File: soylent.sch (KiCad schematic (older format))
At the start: 17 parts, among them J1 DB9_Female, J2 Conn_01x04, J3 Conn_01x04, J4 Conn_02x03_Counter_Clockwise, Q1 BC847BPN, U1 ATtiny202-SS, U2 MIC5504-3.3YM5

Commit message: Add explicit jumper wire
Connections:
- net at C2.1, D1.1 (K), D2.1 (K)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: now also JP2.1 (A), U2.3 (EN)
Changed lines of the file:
@@
 	-1   0    0    -1
 $EndComp
-Wire Wire Line
-	7550 5000 7700 5000
 $Comp
 L power:GND #PWR0103
@@
 Wire Wire Line
 	7450 5300 7650 5300
-Wire Wire Line
-	7650 5300 7650 4800
 Connection ~ 7650 4800
 Wire Wire Line
@@
 Wire Wire Line
 	7900 4800 8000 4800
+Wire Wire Line
+	7650 5300 7650 4800
+Wire Wire Line
+	7550 5000 7700 5000
+Wire Wire Line
+	8000 5000 8000 5200
+Wire Wire Line
+	8000 5200 7700 5200
+Wire Wire Line
+	7700 5200 7700 5000
+Connection ~ 8000 5000
+Connection ~ 7700 5000
 $EndSCHEMATC

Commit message: Pick footprints for remaining items
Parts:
- C1, C2: footprint (none) -> Capacitor_SMD:C_0603_1608Metric
- D1, D2: footprint (none) -> Diode_SMD:D_0603_1608Metric
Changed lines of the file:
@@
 F 0 "C2" V 7048 5300 50  0000 C CNN
 F 1 "1u" V 7139 5300 50  0000 C CNN
-F 2 "" H 7338 5150 50  0001 C CNN
+F 2 "Capacitor_SMD:C_0603_1608Metric" H 7338 5150 50  0001 C CNN
 F 3 "~" H 7300 5300 50  0001 C CNN
 	1    7300 5300
@@
 F 0 "C1" V 6748 5300 50  0000 C CNN
 F 1 "1u" V 6839 5300 50  0000 C CNN
-F 2 "" H 7038 5150 50  0001 C CNN
+F 2 "Capacitor_SMD:C_0603_1608Metric" H 7038 5150 50  0001 C CNN
 F 3 "~" H 7000 5300 50  0001 C CNN
 	1    7000 5300
@@
 F 0 "D1" V 7946 4528 50  0000 L CNN
 F 1 "D" V 7855 4528 50  0000 L CNN
-F 2 "" H 7900 4450 50  0001 C CNN
+F 2 "Diode_SMD:D_0603_1608Metric" H 7900 4450 50  0001 C CNN
 F 3 "~" H 7900 4450 50  0001 C CNN
 	1    7900 4450
@@
 F 0 "D2" V 8096 4471 50  0000 R CNN
 F 1 "D" V 8005 4471 50  0000 R CNN
-F 2 "" H 8050 4550 50  0001 C CNN
+F 2 "Diode_SMD:D_0603_1608Metric" H 8050 4550 50  0001 C CNN
 F 3 "~" H 8050 4550 50  0001 C CNN
 	1    8050 4550

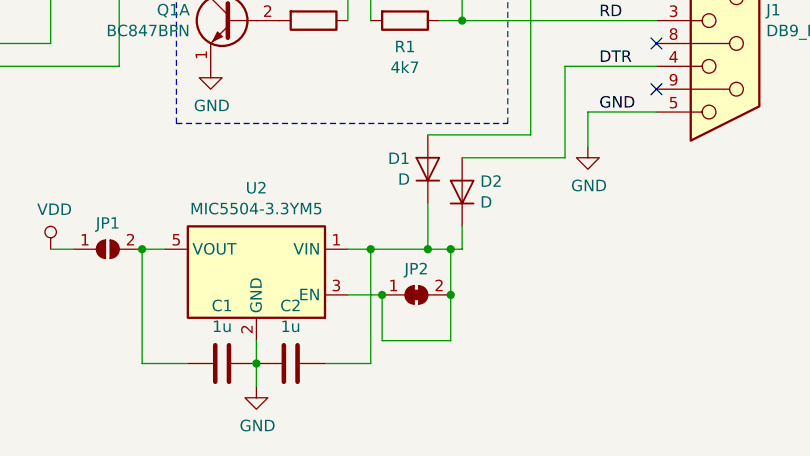
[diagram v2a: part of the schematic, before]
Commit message: Make whole regulator disconnectable
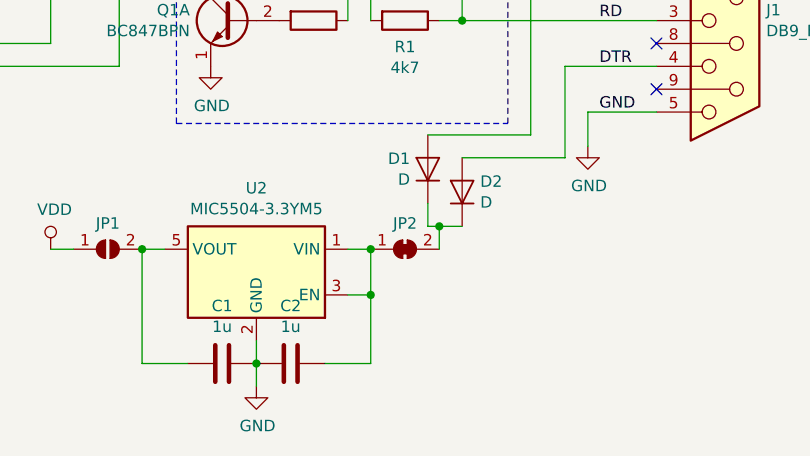
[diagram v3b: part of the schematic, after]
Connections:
- net at C2.1, JP2.1 (A), U2.1 (VIN)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: no longer D1.1 (K), D2.1 (K), JP2.2 (B)
- new net: D1.1 (K), D2.1 (K), JP2.2 (B)
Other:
- moved on the sheet: JP2
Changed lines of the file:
@@
 L Jumper:SolderJumper_2_Bridged JP2
 U 1 1 5DE20E78
-P 7850 5000
-F 0 "JP2" H 7850 5113 50  0000 C CNN
-F 1 "SolderJumper_2_Bridged" H 7850 5114 50  0001 C CNN
-F 2 "Jumpers:SMT-JUMPER_2_NO_SILK" H 7850 5000 50  0001 C CNN
-F 3 "~" H 7850 5000 50  0001 C CNN
-	1    7850 5000
+P 7800 4800
+F 0 "JP2" H 7800 4913 50  0000 C CNN
+F 1 "SolderJumper_2_Bridged" H 7800 4914 50  0001 C CNN
+F 2 "Jumpers:SMT-JUMPER_2_NO_SILK" H 7800 4800 50  0001 C CNN
+F 3 "~" H 7800 4800 50  0001 C CNN
+	1    7800 4800
 	1    0    0    -1
 $EndComp
-Wire Wire Line
-	8000 5000 8000 4800
 Wire Wire Line
 	7550 4800 7650 4800
@@
 Wire Wire Line
 	7450 5300 7650 5300
-Connection ~ 7650 4800
-Wire Wire Line
-	7650 4800 7900 4800
 $Comp
 L Device:D D1
@@
 $EndComp
 Wire Wire Line
-	8050 4700 8050 4800
+	7650 5300 7650 5000
 Wire Wire Line
-	8050 4800 8000 4800
-Connection ~ 8000 4800
+	7900 4600 7900 4700
 Wire Wire Line
-	7900 4600 7900 4800
-Connection ~ 7900 4800
+	7900 4700 7950 4700
 Wire Wire Line
-	7900 4800 8000 4800
+	7550 5000 7650 5000
+Connection ~ 7650 5000
 Wire Wire Line
-	7650 5300 7650 4800
+	7650 5000 7650 4800
+Connection ~ 7650 4800
 Wire Wire Line
-	7550 5000 7700 5000
+	7950 4700 7950 4800
+Connection ~ 7950 4700
 Wire Wire Line
-	8000 5000 8000 5200
-Wire Wire Line
-	8000 5200 7700 5200
-Wire Wire Line
-	7700 5200 7700 5000
-Connection ~ 8000 5000
-Connection ~ 7700 5000
+	7950 4700 8050 4700
 $EndSCHEMATC

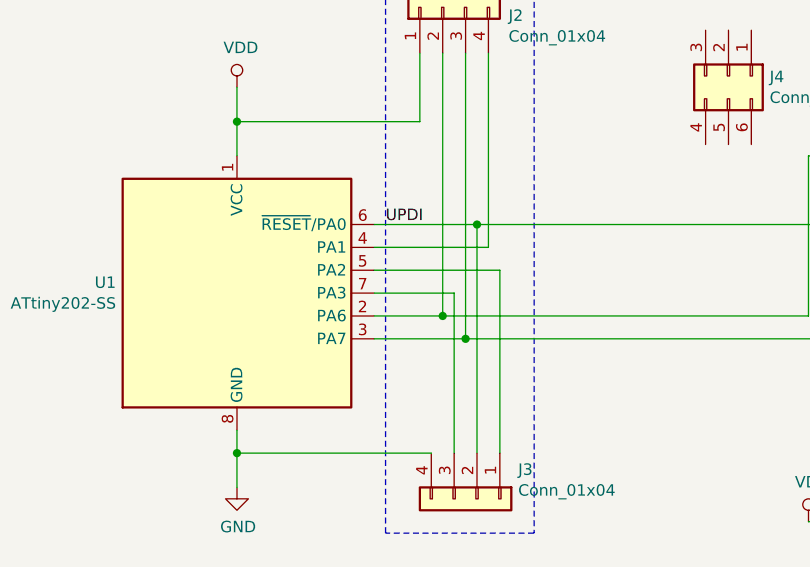
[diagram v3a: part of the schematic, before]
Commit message: Move breakout traces to bottom layer
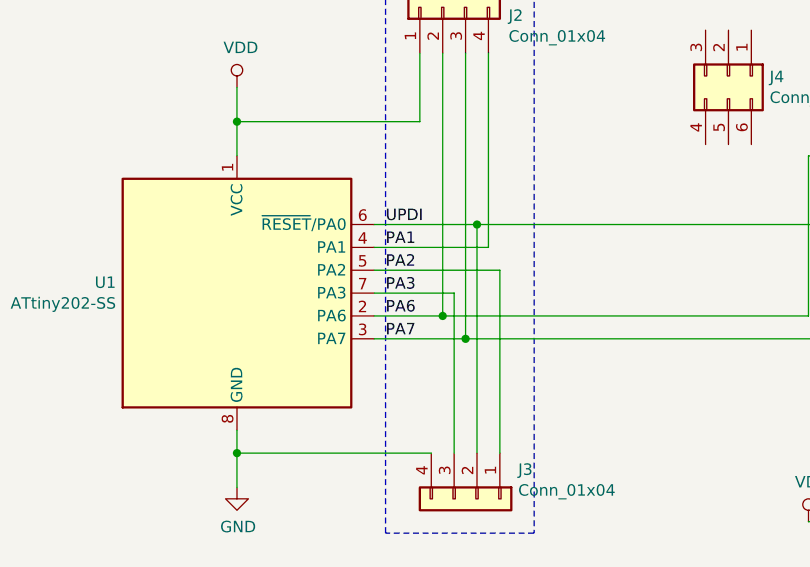
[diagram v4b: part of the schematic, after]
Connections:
- net PA6: now reaches J2.2 (Pin_2), R4.2, U1.2 (PA6)
- net PA7: now reaches J2.3 (Pin_3), Q1.6 (C1), R2.1, U1.3 (PA7)
- net PA1: now reaches J2.4 (Pin_4), U1.4 (PA1)
- net PA2: now reaches J3.1 (Pin_1), U1.5 (PA2)
- net PA3: now reaches J3.3 (Pin_3), U1.7 (PA3)
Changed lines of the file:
@@
 Wire Wire Line
 	7950 4700 8050 4700
+Text Label 4400 3600 0    50   ~ 0
+PA1
+Text Label 4400 3700 0    50   ~ 0
+PA2
+Text Label 4400 3800 0    50   ~ 0
+PA3
+Text Label 4400 3900 0    50   ~ 0
+PA6
+Text Label 4400 4000 0    50   ~ 0
+PA7
 $EndSCHEMATC

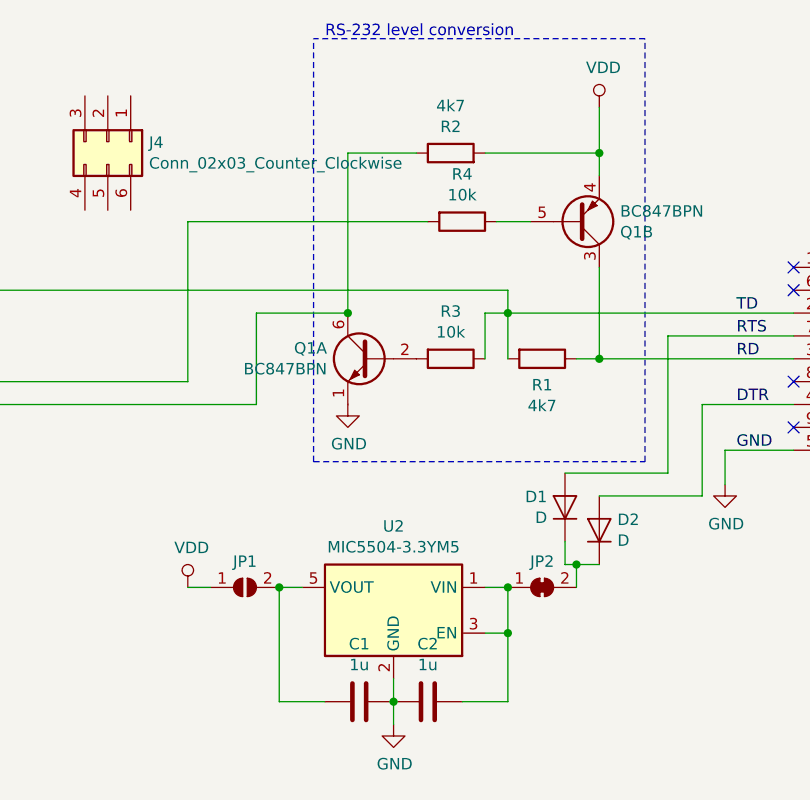
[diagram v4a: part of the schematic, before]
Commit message: Add a box for parasitic power
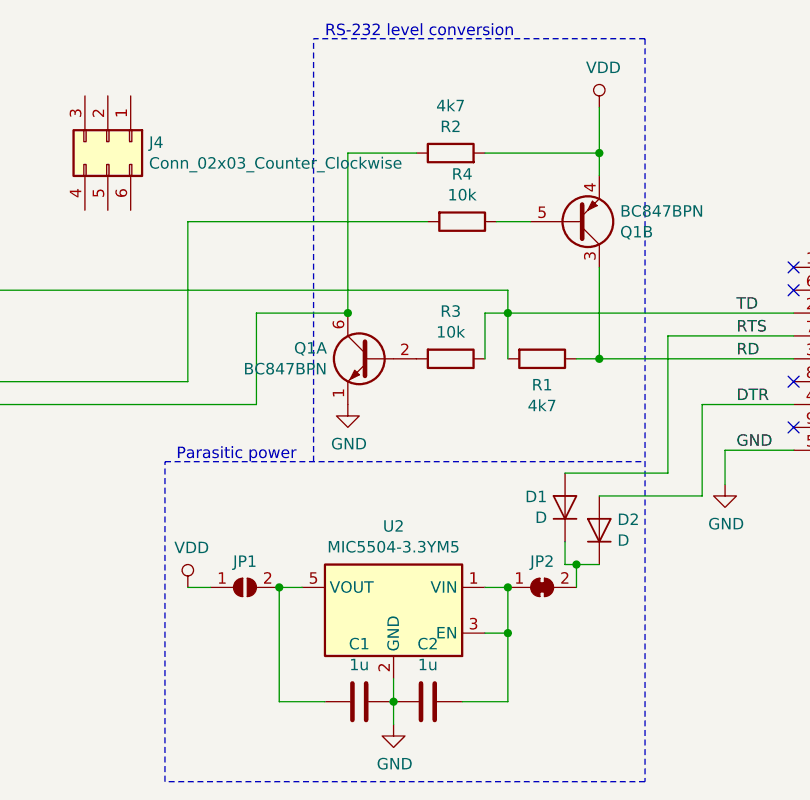
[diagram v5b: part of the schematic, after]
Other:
- note added: "Parasitic power"
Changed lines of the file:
@@
 Connection ~ 8050 2900
-Wire Notes Line
-	6800 4250 8250 4250
-Wire Notes Line
-	8250 4250 8250 2400
 Wire Notes Line
 	8250 2400 6800 2400
@@
 Text Label 4400 4000 0    50   ~ 0
 PA7
+Wire Notes Line
+	8250 5650 6150 5650
+Wire Notes Line
+	6150 5650 6150 4250
+Wire Notes Line
+	6150 4250 8250 4250
+Wire Notes Line
+	8250 2400 8250 5650
+Text Notes 6200 4250 0    50   ~ 0
+Parasitic power
 $EndSCHEMATC

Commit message: Cleanup and prep for TTY I/F
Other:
- note added: "TTY interface"
- moved on the sheet: J4, R4
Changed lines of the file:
@@
 L Connector_Generic:Conn_02x03_Counter_Clockwise J4
 U 1 1 5DDE85A2
-P 5900 2850
-F 0 "J4" V 5904 3030 50  0000 L CNN
-F 1 "Conn_02x03_Counter_Clockwise" V 5995 3030 50  0000 L CNN
-F 2 "Pin_Headers:Pin_Header_Straight_2x03_Pitch2.54mm" H 5900 2850 50  0001 C CNN
-F 3 "~" H 5900 2850 50  0001 C CNN
-	1    5900 2850
-	0    1    1    0
+P 6200 2700
+F 0 "J4" H 6250 2925 50  0000 C CNN
+F 1 "Conn_02x03_Counter_Clockwise" V 6295 2880 50  0001 L CNN
+F 2 "Pin_Headers:Pin_Header_Straight_2x03_Pitch2.54mm" H 6200 2700 50  0001 C CNN
+F 3 "~" H 6200 2700 50  0001 C CNN
+	1    6200 2700
+	1    0    0    1
 $EndComp
 Wire Wire Line
@@
 U 1 1 5DDFC6FD
 P 7400 2900
-F 0 "R2" V 7515 2900 50  0000 C CNN
-F 1 "4k7" V 7606 2900 50  0000 C CNN
+F 0 "R2" V 7607 2900 50  0000 C CNN
+F 1 "4k7" V 7516 2900 50  0000 C CNN
 F 2 "Resistors_SMD:R_0603_HandSoldering" V 7330 2900 50  0001 C CNN
 F 3 "~" H 7400 2900 50  0001 C CNN
@@
 	1    0    0    -1
 $EndComp
-Wire Wire Line
-	4650 3900 6250 3900
 Connection ~ 4650 3900
 Wire Wire Line
@@
 	8050 3400 8050 3800
 Connection ~ 6950 3600
-Wire Wire Line
-	6250 3900 6250 3200
 Wire Wire Line
 	6950 2900 7250 2900
@@
 L Device:R R4
 U 1 1 5DDEECC2
-P 7450 3200
-F 0 "R4" V 7243 3200 50  0000 C CNN
-F 1 "10k" V 7334 3200 50  0000 C CNN
-F 2 "Resistors_SMD:R_0603_HandSoldering" V 7380 3200 50  0001 C CNN
-F 3 "~" H 7450 3200 50  0001 C CNN
-	1    7450 3200
+P 7400 3200
+F 0 "R4" V 7193 3200 50  0000 C CNN
+F 1 "10k" V 7284 3200 50  0000 C CNN
+F 2 "Resistors_SMD:R_0603_HandSoldering" V 7330 3200 50  0001 C CNN
+F 3 "~" H 7400 3200 50  0001 C CNN
+	1    7400 3200
 	0    1    1    0
 $EndComp
-Wire Wire Line
-	7750 3200 7600 3200
-Wire Wire Line
-	6250 3200 7300 3200
 $Comp
 L Device:R R3
@@
 Text Notes 6200 4250 0    50   ~ 0
 Parasitic power
+Wire Notes Line
+	5150 2400 6700 2400
+Wire Notes Line
+	6700 2400 6700 4100
+Wire Notes Line
+	6700 4100 5150 4100
+Wire Notes Line
+	5150 4100 5150 2400
+Wire Wire Line
+	6450 3900 6450 3200
+Wire Wire Line
+	6450 3200 7250 3200
+Wire Wire Line
+	4650 3900 6450 3900
+Wire Wire Line
+	7550 3200 7750 3200
+Text Notes 5200 2400 0    50   ~ 0
+TTY interface
 $EndSCHEMATC

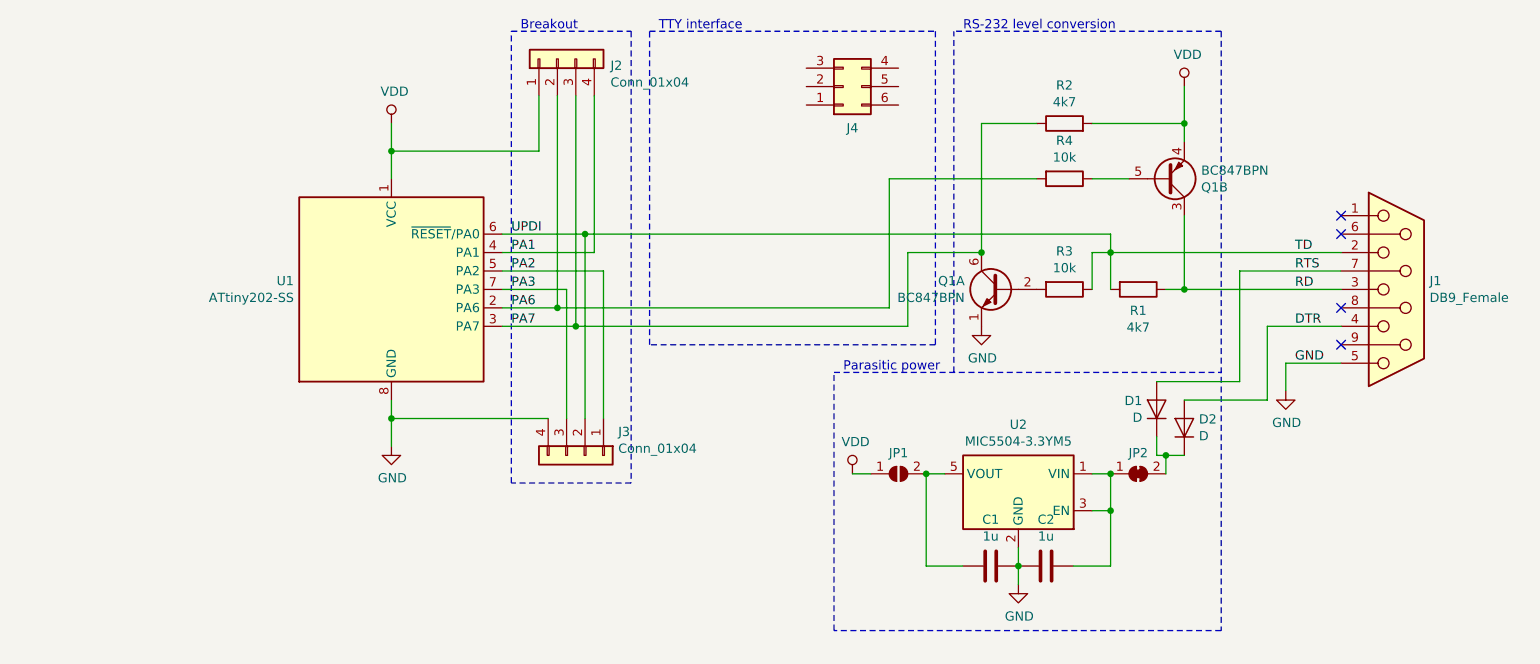
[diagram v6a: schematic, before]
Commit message: Adding components for TTY
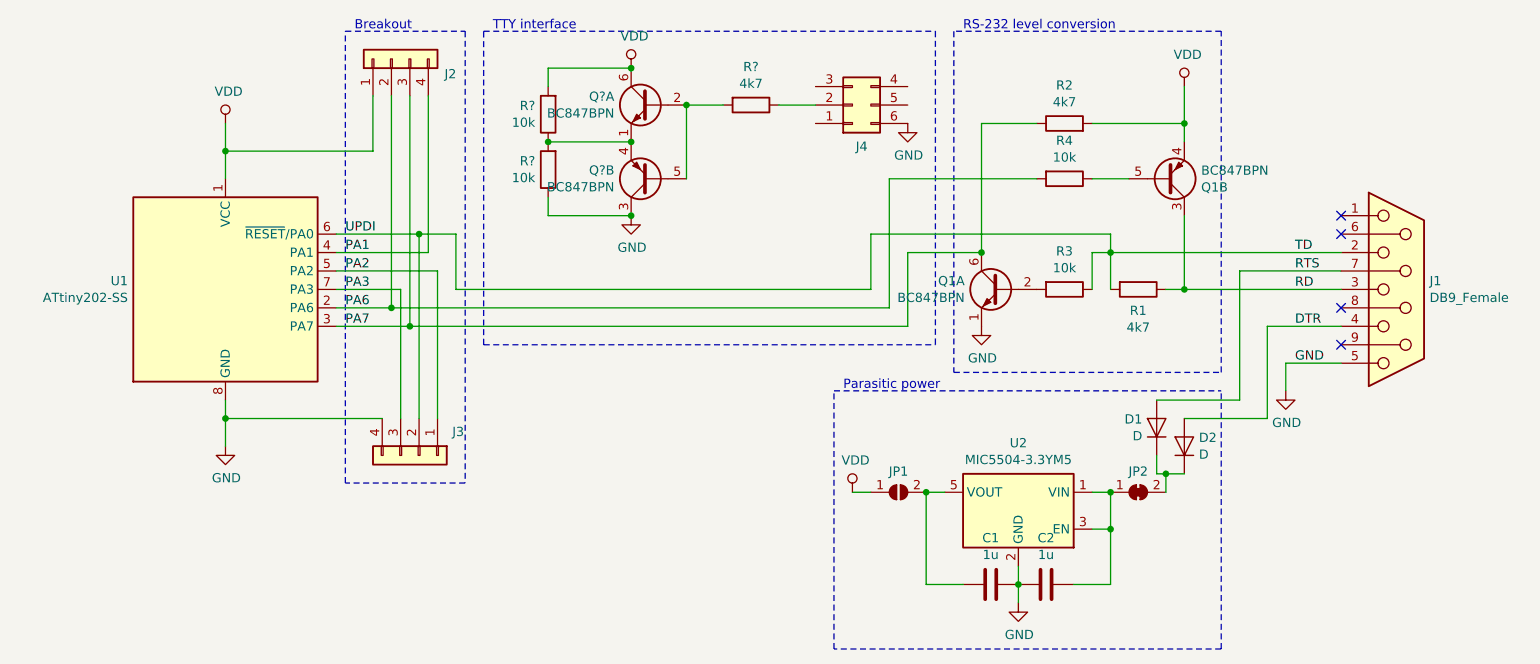
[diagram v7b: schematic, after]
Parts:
- added Q? (x2): BC847BPN, TO_SOT_Packages_SMD:SOT-363_SC-70-6_Handsoldering, symbol Transistor_BJT:BC847BPN
- added R?: 4k7, Resistors_SMD:R_0603_HandSoldering, symbol Device:R
- added R? (x2): 10k, Resistors_SMD:R_0603_HandSoldering, symbol Device:R
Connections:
- net GND: now also J4.6 (Pin_6), Q?.3 (C2), R?.1
- net VDD: now also Q?.6 (C1), R?.2
- net at J4.2 (Pin_2): now also R?.1
- new net: Q?.2 (B1), Q?.5 (B2), R?.2
- new net: Q?.1 (E1), Q?.4 (E2), R?.1, R?.2
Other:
- moved on the sheet: C1, C2, D1, D2, J2, J3, J4, JP1, JP2, U1, U2

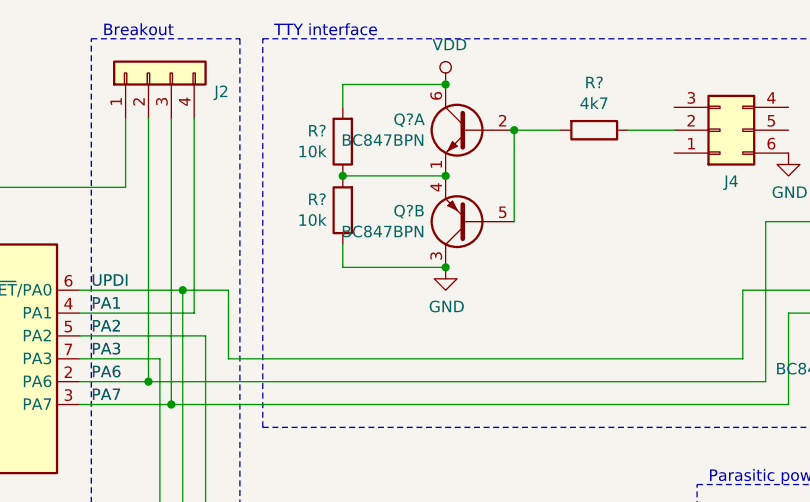
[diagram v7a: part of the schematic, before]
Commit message: Hook up analog in
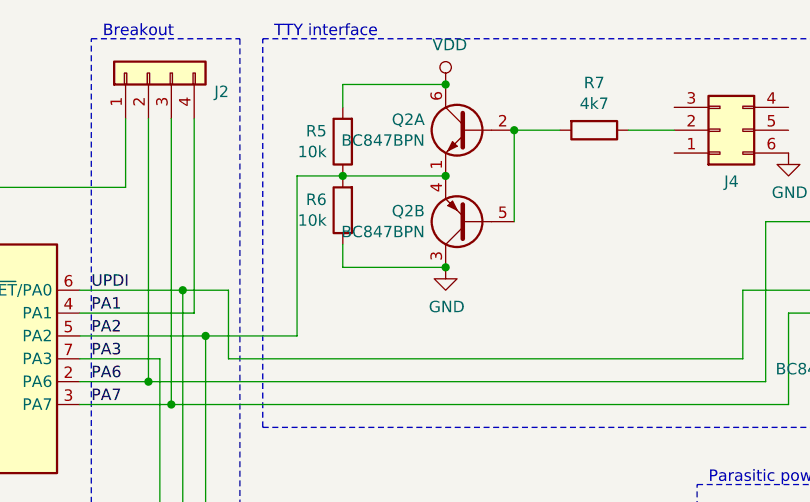
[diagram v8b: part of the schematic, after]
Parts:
- gave numbers to parts that had none: 4
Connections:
- net PA2: now also Q2.1 (E1), Q2.4 (E2), R5.1, R6.2
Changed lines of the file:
@@
 $EndComp
 $Comp
-L Device:R R?
+L Device:R R7
 U 1 1 5DEFDFE7
 P 5700 2800
-F 0 "R?" V 5493 2800 50  0000 C CNN
+F 0 "R7" V 5493 2800 50  0000 C CNN
 F 1 "4k7" V 5584 2800 50  0000 C CNN
 F 2 "Resistors_SMD:R_0603_HandSoldering" V 5630 2800 50  0001 C CNN
@@
 $EndComp
 $Comp
-L Transistor_BJT:BC847BPN Q?
+L Transistor_BJT:BC847BPN Q2
 U 2 1 5DF05573
 P 5150 3200
-F 0 "Q?" H 5341 3154 50  0000 L CNN
+F 0 "Q2" H 5341 3154 50  0000 L CNN
 F 1 "BC847BPN" H 5341 3245 50  0000 L CNN
 F 2 "TO_SOT_Packages_SMD:SOT-363_SC-70-6_Handsoldering" H 5350 3300 50  0001 C CNN
@@
 $EndComp
 $Comp
-L Transistor_BJT:BC847BPN Q?
+L Transistor_BJT:BC847BPN Q2
 U 1 1 5DF18897
 P 5150 2800
-F 0 "Q?" H 5341 2846 50  0000 L CNN
+F 0 "Q2" H 5341 2846 50  0000 L CNN
 F 1 "BC847BPN" H 5341 2755 50  0000 L CNN
 F 2 "TO_SOT_Packages_SMD:SOT-363_SC-70-6_Handsoldering" H 5350 2900 50  0001 C CNN
@@
 Connection ~ 3900 3500
 $Comp
-L power:VDD #PWR?
+L power:VDD #PWR0109
 U 1 1 5DF48DE3
 P 5050 2600
-F 0 "#PWR?" H 5050 2450 50  0001 C CNN
+F 0 "#PWR0109" H 5050 2450 50  0001 C CNN
 F 1 "VDD" H 5068 2773 50  0000 C CNN
 F 2 "" H 5050 2600 50  0001 C CNN
@@
 $EndComp
 $Comp
-L power:GND #PWR?
+L power:GND #PWR0110
 U 1 1 5DF492BB
 P 5050 3400
-F 0 "#PWR?" H 5050 3150 50  0001 C CNN
+F 0 "#PWR0110" H 5050 3150 50  0001 C CNN
 F 1 "GND" H 5055 3227 50  0000 C CNN
 F 2 "" H 5050 3400 50  0001 C CNN
@@
 	5850 2800 6050 2800
 $Comp
-L Device:R R?
+L Device:R R5
 U 1 1 5DF5183F
 P 4600 2850
-F 0 "R?" H 4670 2804 50  0000 L CNN
+F 0 "R5" H 4670 2804 50  0000 L CNN
 F 1 "10k" H 4670 2895 50  0000 L CNN
 F 2 "Resistors_SMD:R_0603_HandSoldering" V 4530 2850 50  0001 C CNN
@@
 $EndComp
 $Comp
-L Device:R R?
+L Device:R R6
 U 1 1 5DF52A36
 P 4600 3150
-F 0 "R?" H 4670 3104 50  0000 L CNN
+F 0 "R6" H 4670 3104 50  0000 L CNN
 F 1 "10k" H 4670 3195 50  0000 L CNN
 F 2 "Resistors_SMD:R_0603_HandSoldering" V 4530 3150 50  0001 C CNN
@@
 Wire Notes Line
 	8250 4250 8250 2400
+Wire Wire Line
+	4000 3700 4400 3700
+Wire Wire Line
+	4400 3700 4400 3000
+Wire Wire Line
+	4400 3000 4600 3000
+Connection ~ 4000 3700
 $EndSCHEMATC
